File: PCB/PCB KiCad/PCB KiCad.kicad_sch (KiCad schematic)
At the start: 0 parts

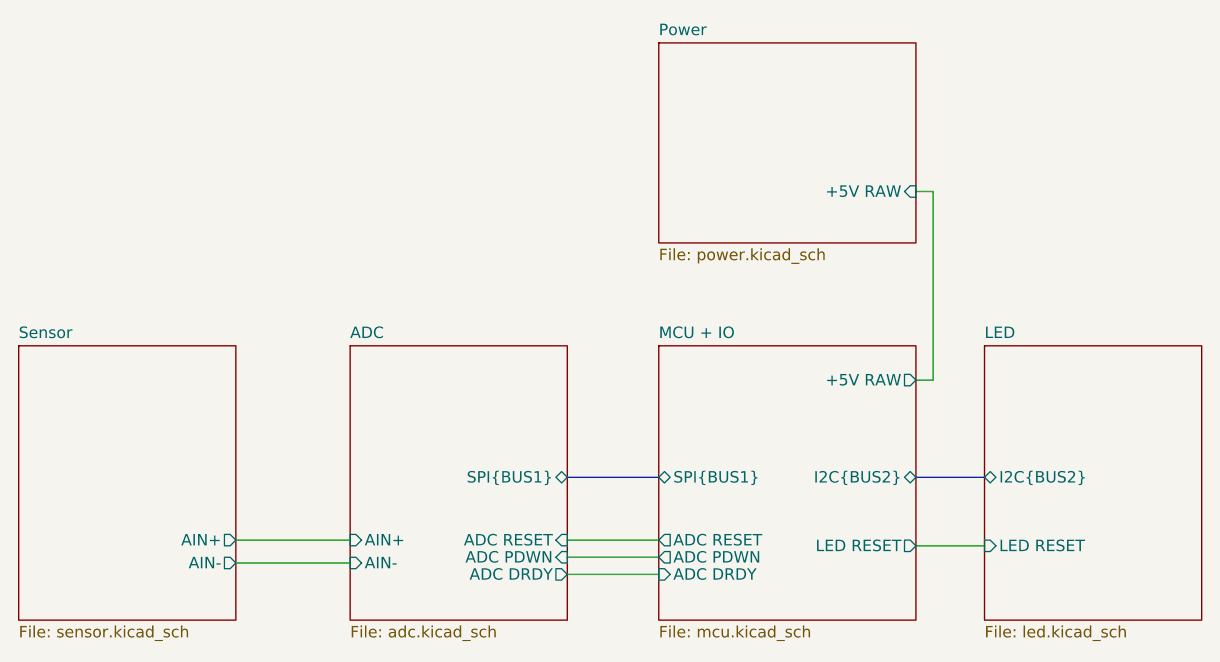
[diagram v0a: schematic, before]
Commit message: added esp32c3
Signed-off-by: Lawrence Kincheloe <lawrence.kincheloe@mavericktechok.com>
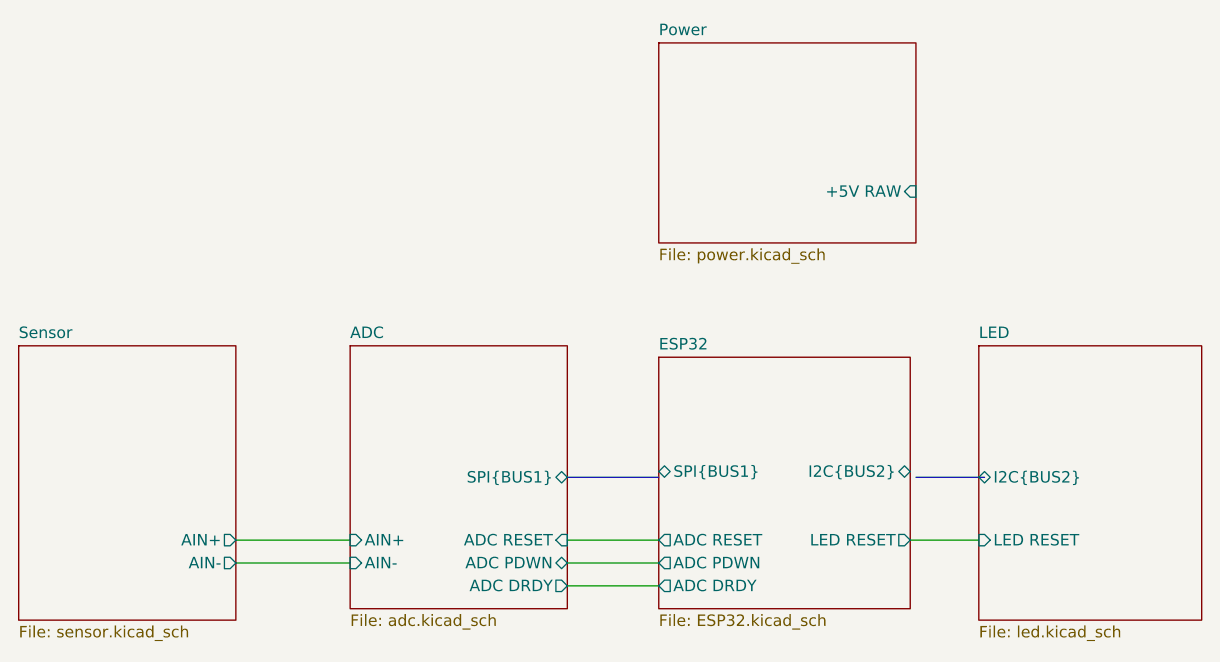
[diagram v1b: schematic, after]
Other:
- removed sheet MCU + IO
- added sheet ESP32 (ESP32.kicad_sch)
